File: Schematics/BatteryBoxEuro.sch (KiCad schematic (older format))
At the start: 20 parts, among them J1 , J2 , J3 , J4 , K1 JD2912-1Z-12VDC_40A, U1 Terminal16, U2 F_Distributor, U3 PB12V-Charger, U4 DPlusSimulator, U5 Pulser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

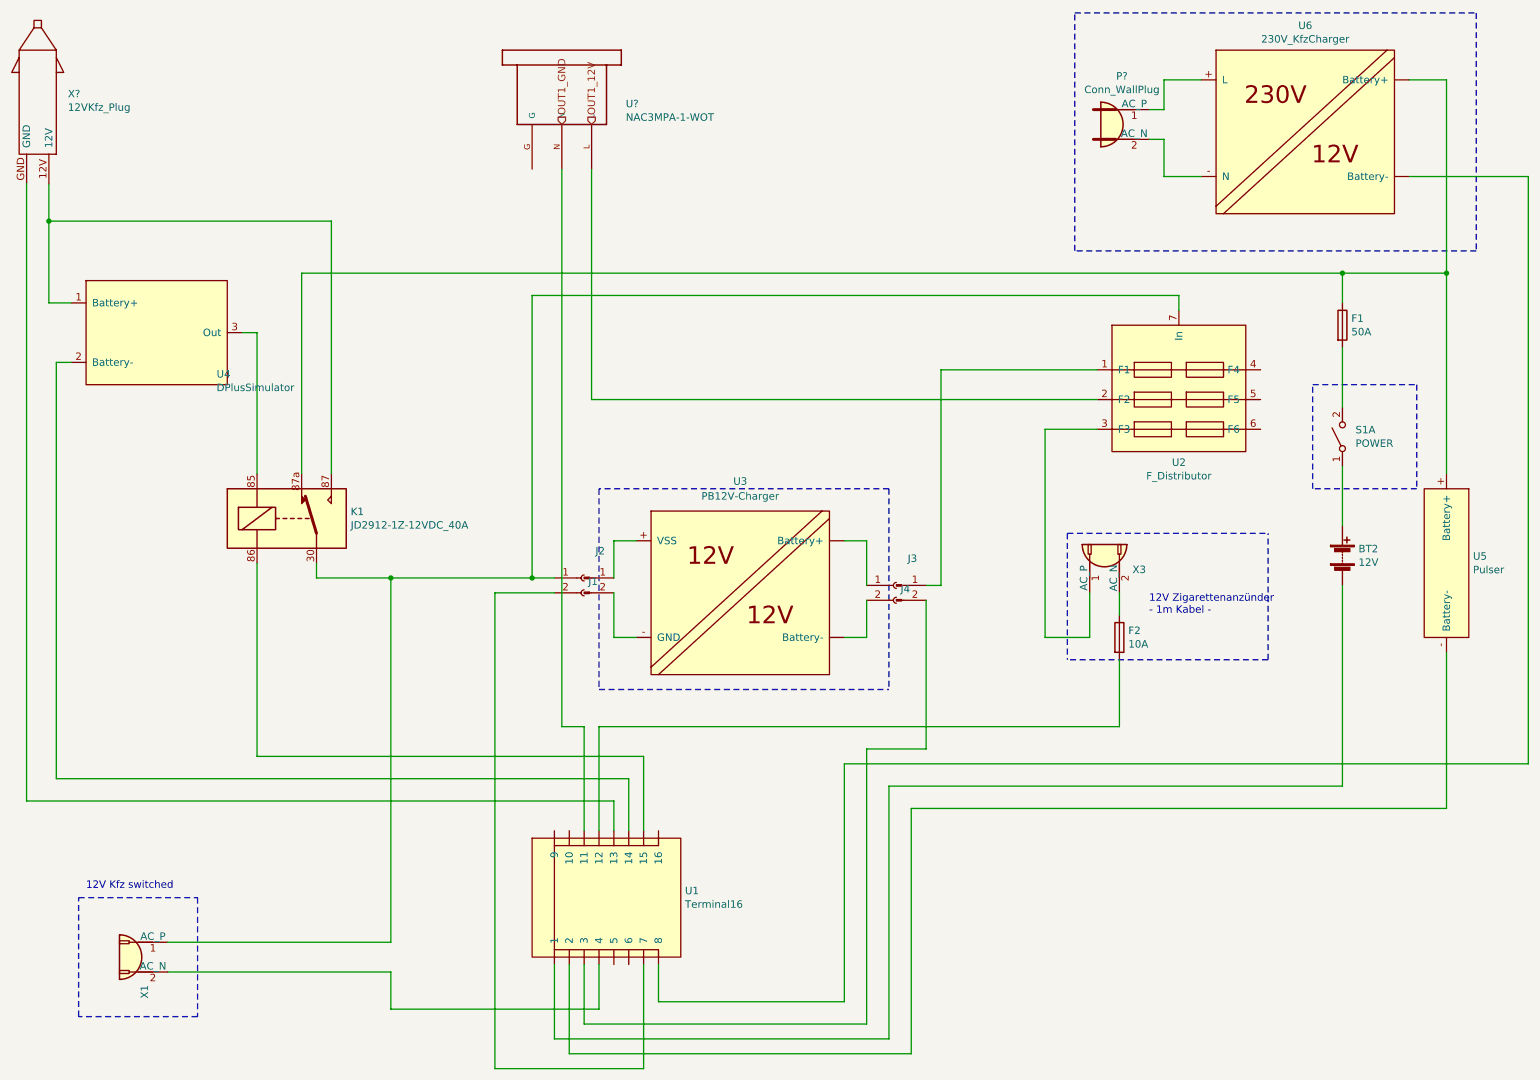
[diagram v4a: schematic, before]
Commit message: rearrange symbols
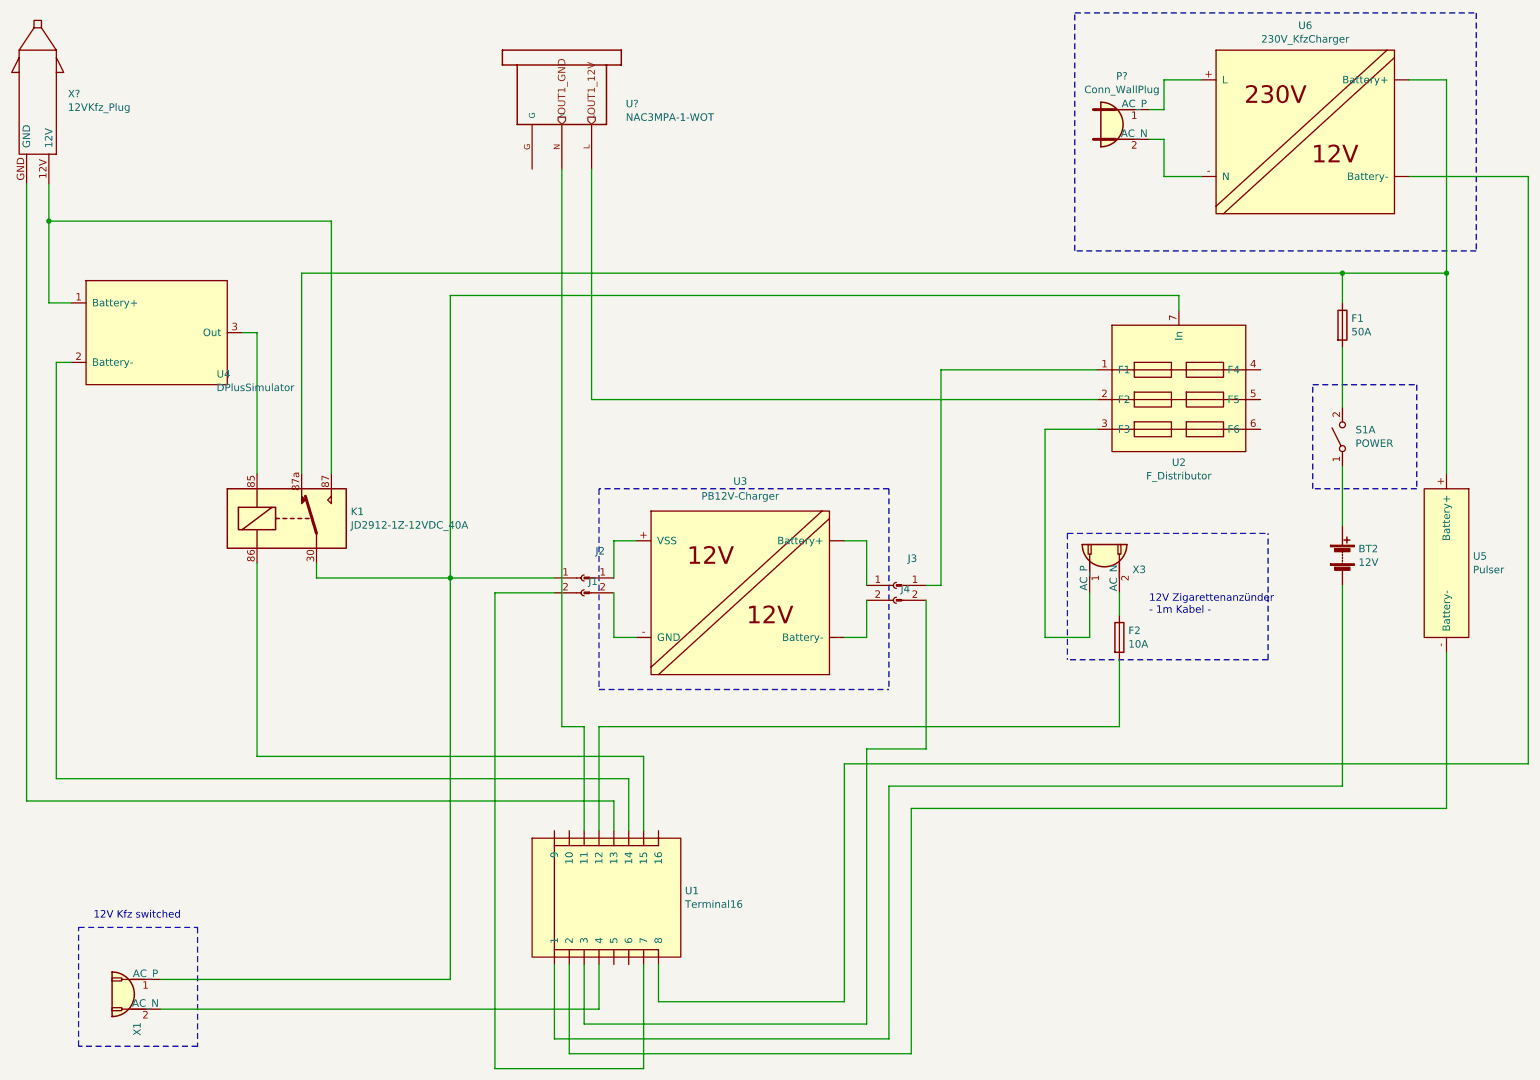
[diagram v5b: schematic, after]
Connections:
- net at U1.~ (9): now also X?.GND
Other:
- moved on the sheet: X1
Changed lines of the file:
@@
 12V Zigarettenanzünder\n- 1m Kabel -
 Wire Wire Line
-	3200 4400 4150 4400
-Wire Wire Line
-	3200 7300 4600 7300
-Wire Wire Line
 	4600 7300 4600 7000
-Wire Notes Line
-	1100 6550 1900 6550
-Wire Notes Line
-	1900 6550 1900 7350
-Wire Notes Line
-	1900 7350 1100 7350
-Wire Notes Line
-	1100 7350 1100 6550
-Text Notes 1150 6500 0    50   ~ 0
-12V Kfz switched
 Wire Notes Line
 	4600 3800 4600 5150
@@
 	1    0    0    -1
 $EndComp
-Connection ~ 3200 4400
+Connection ~ 3600 4400
 Text HLabel 4550 1350 1    50   Input ~ 0
 OUT1_12V
@@
 $EndComp
 Wire Wire Line
-	4150 4400 4150 2500
-Wire Wire Line
-	4150 2500 8500 2500
+	3600 4400 3600 2500
 Wire Wire Line
 	8500 2500 8500 2600
-Connection ~ 4150 4400
-Wire Wire Line
-	4150 4400 4300 4400
 Connection ~ 9600 2350
 Wire Wire Line
@@
 	2700 4300 2700 4400
 Wire Wire Line
-	2700 4400 3200 4400
+	2700 4400 3600 4400
 Wire Wire Line
 	2300 5600 2300 4300
@@
 	2300 2750 2300 3700
 Wire Wire Line
-	3200 4400 3200 6850
+	3600 4400 4300 4400
+Wire Wire Line
+	3600 2500 8500 2500
 $Comp
 L Connector:Conn_WallSocket X1
 U 1 1 5EC190DC
-P 1500 6950
-F 0 "X1" V 1456 6762 50  0000 R CNN
-F 1 "X3" V 1411 6762 50  0001 R CNN
-F 2 "" H 1100 6950 50  0001 C CNN
-F 3 "~" H 1100 6950 50  0001 C CNN
-	1    1500 6950
+P 1450 7200
+F 0 "X1" V 1406 7012 50  0000 R CNN
+F 1 "X3" V 1361 7012 50  0001 R CNN
+F 2 "" H 1050 7200 50  0001 C CNN
+F 3 "~" H 1050 7200 50  0001 C CNN
+	1    1450 7200
 	-1   0    0    -1
 $EndComp
+Text Notes 1200 6700 0    50   ~ 0
+12V Kfz switched
+Wire Notes Line
+	1100 7550 1100 6750
+Wire Notes Line
+	1900 7550 1100 7550
+Wire Notes Line
+	1900 6750 1900 7550
+Wire Notes Line
+	1100 6750 1900 6750
 Wire Wire Line
-	1700 6850 3200 6850
+	1650 7300 4600 7300
 Wire Wire Line
-	3200 7050 3200 7300
+	1650 7100 3600 7100
 Wire Wire Line
-	1700 7050 3200 7050
+	3600 4400 3600 7100
 $EndSCHEMATC

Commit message: remove charger
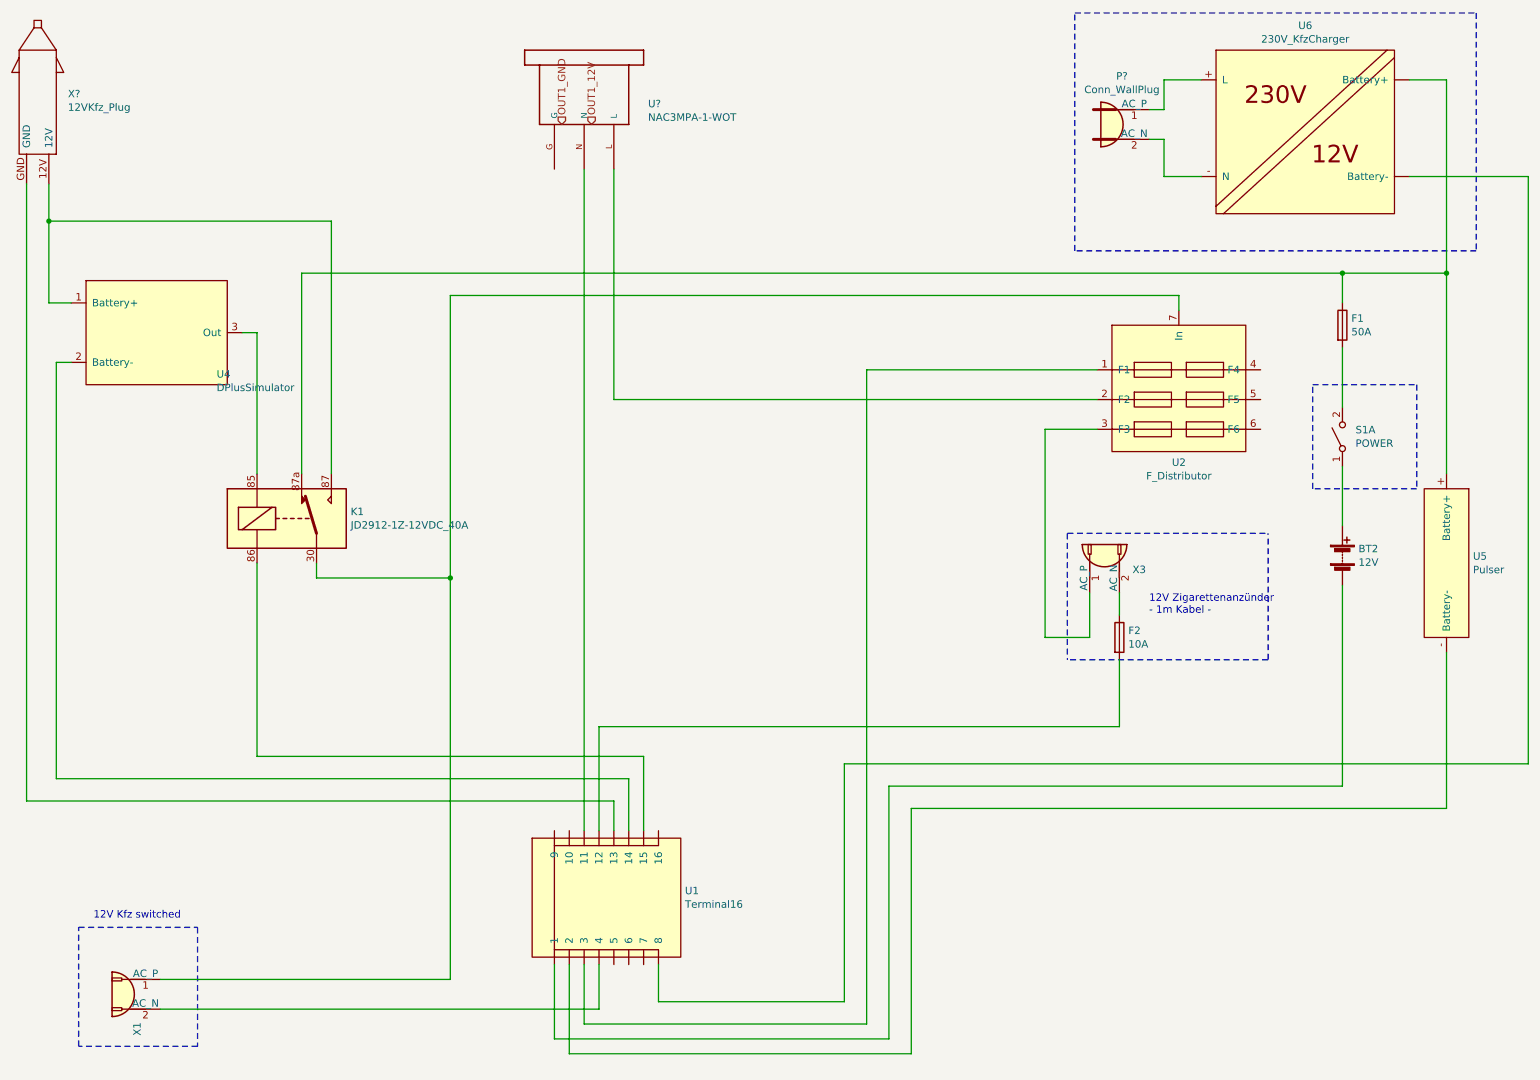
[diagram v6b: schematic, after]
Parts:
- removed J1, J4: (no value), symbol Connector:Conn_01x02_Female
- removed J2, J3: (no value), symbol Connector:Conn_01x02_Male
- removed U3: PB12V-Charger, symbol MyParts:PB12V-Charger
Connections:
- net at U2.1 (F1): now also U1.~ (9)
- net at U1.~ (9): now also X?.GND
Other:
- moved on the sheet: U?
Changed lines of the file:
@@
 	9600 2850 9600 3250
-$Comp
-L MyParts:PB12V-Charger U3
-U 1 1 5E8B48DF
-P 5350 3850
-F 0 "U3" H 5550 3950 50  0000 C CNN
-F 1 "PB12V-Charger" H 5550 3850 50  0000 C CNN
-F 2 "" H 5350 3850 50  0001 C CNN
-F 3 "" H 5350 3850 50  0001 C CNN
-	1    5350 3850
-	1    0    0    -1
-$EndComp
 $Comp
 L MyParts:Terminal16 U1
@@
 	0    -1   -1   0
 $EndComp
-$Comp
-L Connector:Conn_01x02_Female J1
-U 1 1 5E8F0E10
-P 4500 4400
-F 0 "J1" H 4528 4376 50  0000 L CNN
-F 1 " " H 4528 4285 50  0000 L CNN
-F 2 "" H 4500 4400 50  0001 C CNN
-F 3 "~" H 4500 4400 50  0001 C CNN
-	1    4500 4400
-	1    0    0    -1
-$EndComp
-$Comp
-L Connector:Conn_01x02_Male J2
-U 1 1 5E8F155C
-P 4500 4400
-F 0 "J2" H 4608 4581 50  0000 C CNN
-F 1 " " H 4608 4490 50  0000 C CNN
-F 2 "" H 4500 4400 50  0001 C CNN
-F 3 "~" H 4500 4400 50  0001 C CNN
-	1    4500 4400
-	1    0    0    -1
-$EndComp
-Wire Wire Line
-	4700 4400 4700 4150
-Wire Wire Line
-	4700 4150 4850 4150
-Wire Wire Line
-	4700 4500 4700 4800
-Wire Wire Line
-	4700 4800 4850 4800
 Wire Wire Line
 	4300 7500 6550 7500
@@
 	10300 4900 10300 5950
 Wire Wire Line
-	4900 7700 4900 7000
-Wire Wire Line
 	4500 7400 6400 7400
 Wire Wire Line
 	4500 7000 4500 7400
-Wire Wire Line
-	7950 3000 6900 3000
 $Comp
 L Connector:Conn_WallSocket X3
@@
 $EndComp
 Wire Wire Line
-	4500 6100 4500 5400
-Wire Wire Line
 	4600 6100 4600 5400
 Wire Wire Line
@@
 Wire Notes Line
 	9400 3800 9400 3100
-Wire Notes Line
-	6550 3800 4600 3800
-Wire Wire Line
-	6800 4450 6900 4450
-Wire Wire Line
-	6900 3000 6900 4450
-Wire Wire Line
-	6250 4150 6400 4150
-Wire Wire Line
-	6400 4150 6400 4450
 Wire Wire Line
 	7600 3400 7950 3400
 Wire Wire Line
 	4600 5400 8100 5400
-Wire Wire Line
-	6400 5550 6800 5550
-Wire Wire Line
-	6800 5550 6800 4550
-Wire Wire Line
-	6400 5550 6400 7400
-Wire Wire Line
-	6400 4550 6400 4800
-Wire Wire Line
-	6400 4800 6250 4800
-$Comp
-L Connector:Conn_01x02_Male J3
-U 1 1 5EC36685
-P 6600 4450
-F 0 "J3" H 6708 4631 50  0000 C CNN
-F 1 " " H 6708 4540 50  0000 C CNN
-F 2 "" H 6600 4450 50  0001 C CNN
-F 3 "~" H 6600 4450 50  0001 C CNN
-	1    6600 4450
-	1    0    0    -1
-$EndComp
-$Comp
-L Connector:Conn_01x02_Female J4
-U 1 1 5EC3704C
-P 6600 4450
-F 0 "J4" H 6628 4426 50  0000 L CNN
-F 1 " " H 6628 4335 50  0000 L CNN
-F 2 "" H 6600 4450 50  0001 C CNN
-F 3 "~" H 6600 4450 50  0001 C CNN
-	1    6600 4450
-	1    0    0    -1
-$EndComp
 Text Notes 8300 4650 0    50   ~ 0
 12V Zigarettenanzünder\n- 1m Kabel -
 Wire Wire Line
 	4600 7300 4600 7000
-Wire Notes Line
-	4600 3800 4600 5150
-Wire Notes Line
-	6550 3800 6550 5150
-Wire Wire Line
-	3900 7700 4900 7700
-Wire Wire Line
-	3900 4500 4300 4500
-Wire Wire Line
-	3900 4500 3900 7700
 $Comp
 L MyParts:230V_KfzCharger U6
@@
 Wire Wire Line
 	10300 2350 10300 3700
-Wire Notes Line
-	4600 5150 6550 5150
-Wire Wire Line
-	4500 5400 4350 5400
 Wire Wire Line
 	10050 1050 10300 1050
@@
 OUT1_GND
 Wire Wire Line
-	4550 3200 7950 3200
+	4700 3200 7950 3200
 $Comp
 L NAC3MPA-1-WOT:NAC3MPA-1-WOT U?
 U 1 1 5EF1E21B
-P 4150 1450
-F 0 "U?" V 3911 2080 50  0000 L CNN
-F 1 "NAC3MPA-1-WOT" V 4002 2080 50  0000 L CNN
-F 2 "NAC3MPA-1-WOT" H 4150 1450 50  0001 L BNN
-F 3 "" H 4150 1450 50  0001 C CNN
-	1    4150 1450
+P 4300 1450
+F 0 "U?" V 4061 2080 50  0000 L CNN
+F 1 "NAC3MPA-1-WOT" V 4152 2080 50  0000 L CNN
+F 2 "NAC3MPA-1-WOT" H 4300 1450 50  0001 L BNN
+F 3 "" H 4300 1450 50  0001 C CNN
+	1    4300 1450
 	0    1    1    0
 $EndComp
 Wire Wire Line
-	4550 3200 4550 1650
-Wire Wire Line
-	4350 1650 4350 5400
+	4700 3200 4700 1650
 $Comp
 L Connector:Conn_WallPlug P?
@@
 	2300 2750 2300 3700
 Wire Wire Line
-	3600 4400 4300 4400
-Wire Wire Line
 	3600 2500 8500 2500
 $Comp
@@
 Wire Wire Line
 	3600 4400 3600 7100
+Wire Wire Line
+	6400 3000 7950 3000
+Wire Wire Line
+	6400 3000 6400 7400
+Wire Wire Line
+	4500 1650 4500 6100
 $EndSCHEMATC

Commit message: add 2nd plug
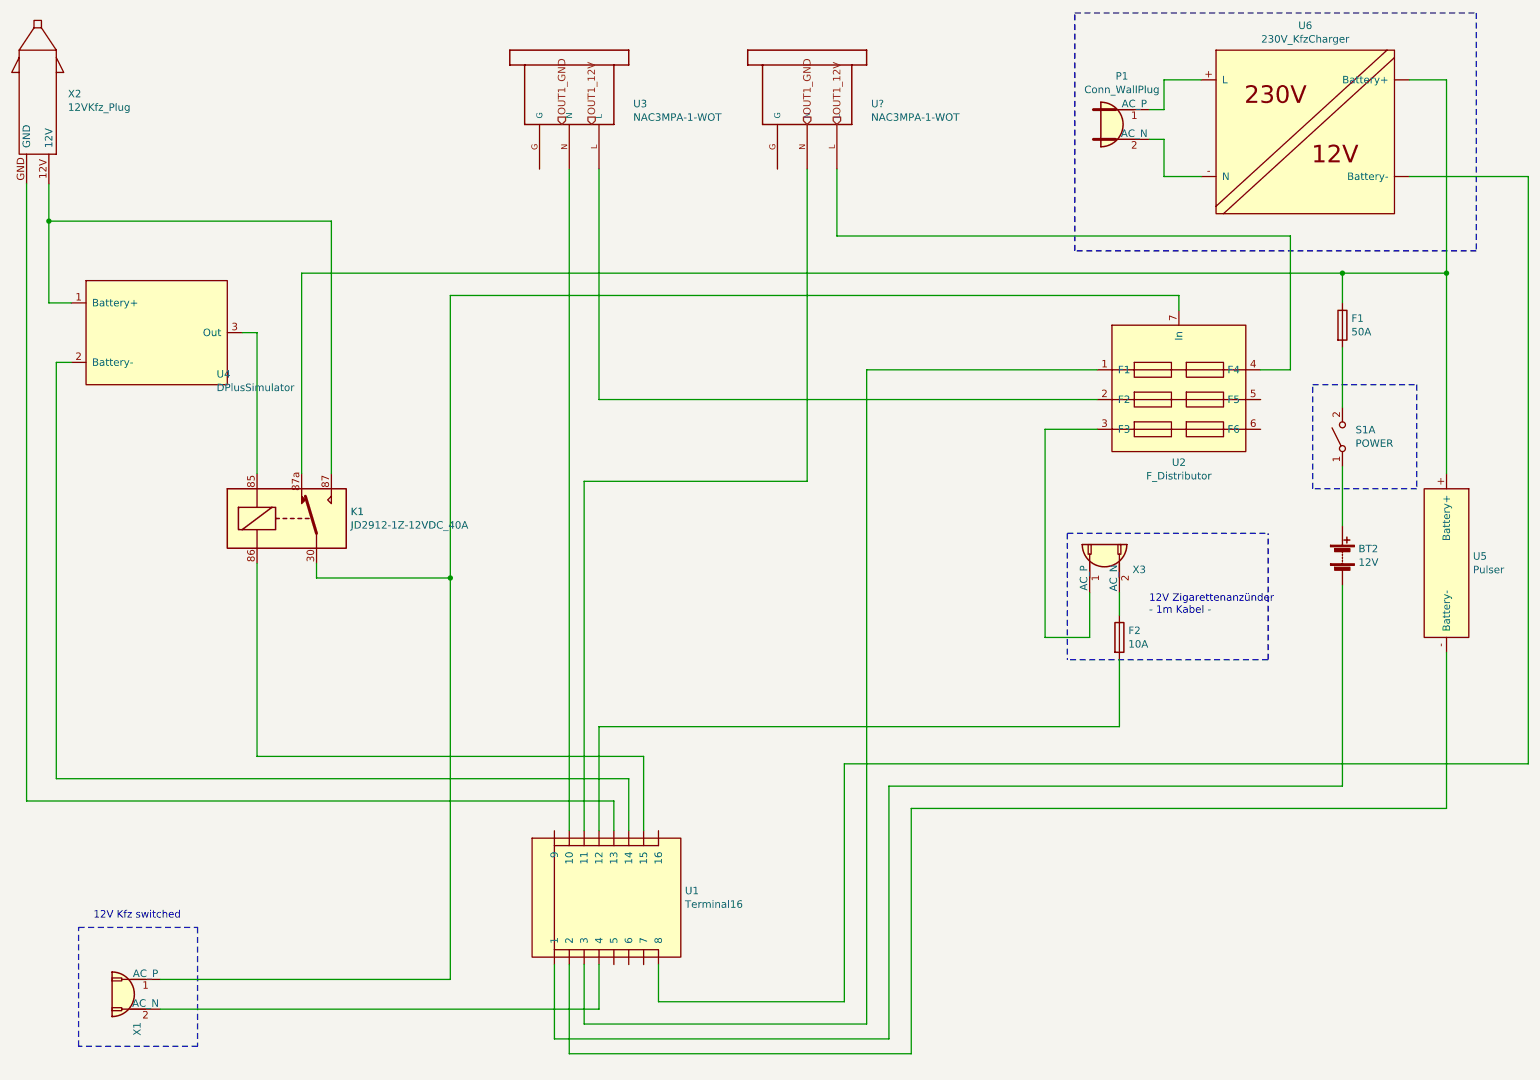
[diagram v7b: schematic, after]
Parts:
- added U?: NAC3MPA-1-WOT, NAC3MPA-1-WOT, symbol NAC3MPA-1-WOT:NAC3MPA-1-WOT
- gave numbers to parts that had none: 3
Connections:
- net at U2.4 (F4): now also U?.L
- net at U1.~ (9): now also U?.N
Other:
- moved on the sheet: U3
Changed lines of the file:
@@
 OUT1_GND
 Wire Wire Line
-	4700 3200 7950 3200
+	4600 3200 7950 3200
 $Comp
-L NAC3MPA-1-WOT:NAC3MPA-1-WOT U?
+L NAC3MPA-1-WOT:NAC3MPA-1-WOT U3
 U 1 1 5EF1E21B
-P 4300 1450
-F 0 "U?" V 4061 2080 50  0000 L CNN
-F 1 "NAC3MPA-1-WOT" V 4152 2080 50  0000 L CNN
-F 2 "NAC3MPA-1-WOT" H 4300 1450 50  0001 L BNN
-F 3 "" H 4300 1450 50  0001 C CNN
-	1    4300 1450
+P 4200 1450
+F 0 "U3" V 3961 2080 50  0000 L CNN
+F 1 "NAC3MPA-1-WOT" V 4052 2080 50  0000 L CNN
+F 2 "NAC3MPA-1-WOT" H 4200 1450 50  0001 L BNN
+F 3 "" H 4200 1450 50  0001 C CNN
+	1    4200 1450
 	0    1    1    0
 $EndComp
 Wire Wire Line
-	4700 3200 4700 1650
+	4600 3200 4600 1650
 $Comp
-L Connector:Conn_WallPlug P?
+L Connector:Conn_WallPlug P1
 U 1 1 5EF29B60
 P 8100 1350
-F 0 "P?" H 8117 1675 50  0000 C CNN
+F 0 "P1" H 8117 1675 50  0000 C CNN
 F 1 "Conn_WallPlug" H 8117 1584 50  0000 C CNN
 F 2 "" H 8500 1350 50  0001 C CNN
@@
 	2800 2000 2800 3700
 $Comp
-L MyParts:12VKfz_Plug X?
+L MyParts:12VKfz_Plug X2
 U 1 1 5EF8167C
 P 1050 1300
-F 0 "X?" V 1206 1278 50  0000 L CNN
+F 0 "X2" V 1206 1278 50  0000 L CNN
 F 1 "12VKfz_Plug" V 1115 1278 50  0000 L CNN
 F 2 "" H 1050 1300 50  0001 C CNN
@@
 	6400 3000 6400 7400
 Wire Wire Line
-	4500 1650 4500 6100
+	4400 1650 4400 6100
+$Comp
+L NAC3MPA-1-WOT:NAC3MPA-1-WOT U?
+U 1 1 5F024C85
+P 5800 1450
+F 0 "U?" V 5561 2080 50  0000 L CNN
+F 1 "NAC3MPA-1-WOT" V 5652 2080 50  0000 L CNN
+F 2 "NAC3MPA-1-WOT" H 5800 1450 50  0001 L BNN
+F 3 "" H 5800 1450 50  0001 C CNN
+	1    5800 1450
+	0    1    1    0
+$EndComp
+Wire Wire Line
+	4500 6100 4500 3750
+Wire Wire Line
+	4500 3750 6000 3750
+Wire Wire Line
+	6000 3750 6000 1650
+Wire Wire Line
+	9050 3000 9250 3000
+Wire Wire Line
+	9250 3000 9250 2100
+Wire Wire Line
+	9250 2100 6200 2100
+Wire Wire Line
+	6200 2100 6200 1650
+Text HLabel 6000 1350 1    50   Input ~ 0
+OUT1_GND
+Text HLabel 6200 1350 1    50   Input ~ 0
+OUT1_12V
 $EndSCHEMATC
